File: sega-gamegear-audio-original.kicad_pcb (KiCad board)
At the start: 2 copper layers, 57 x 31 mm, 20 parts, among them CN1 CONN 2P, CN2 292161-6, IC1 Val**, J1 CONN MINI JACK

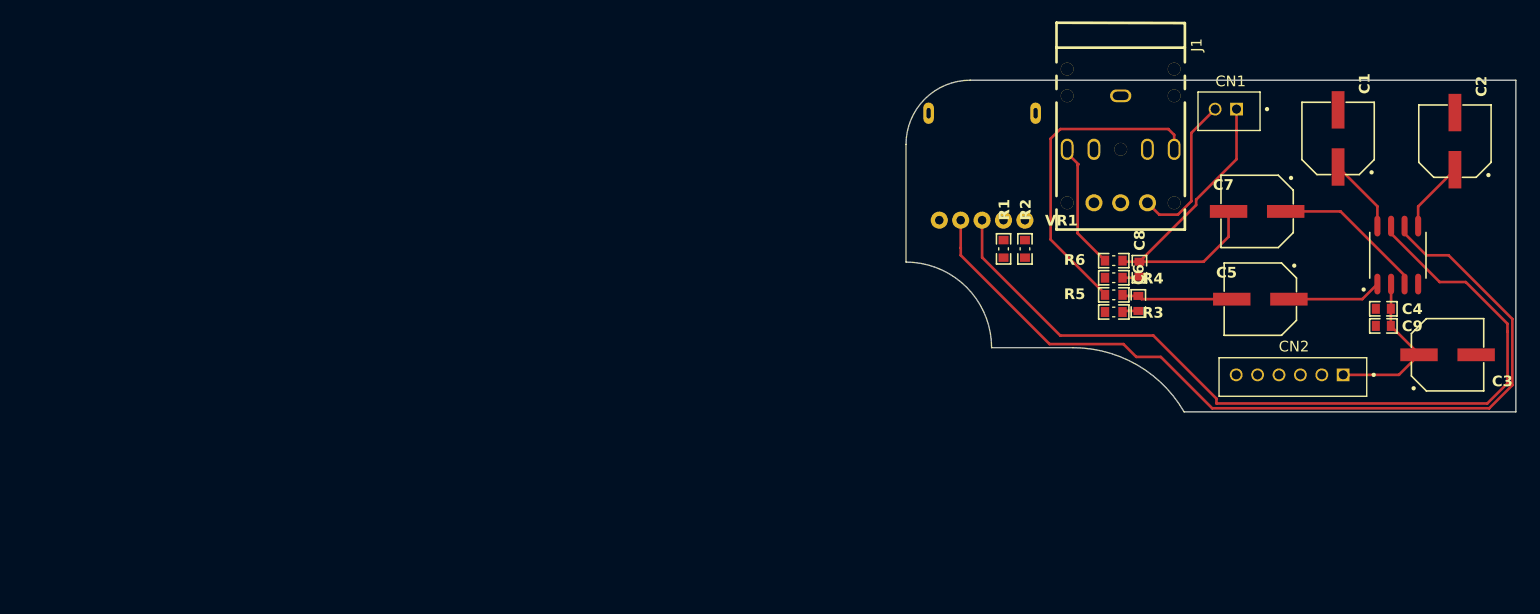
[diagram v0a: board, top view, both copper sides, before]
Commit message: add plated through holes
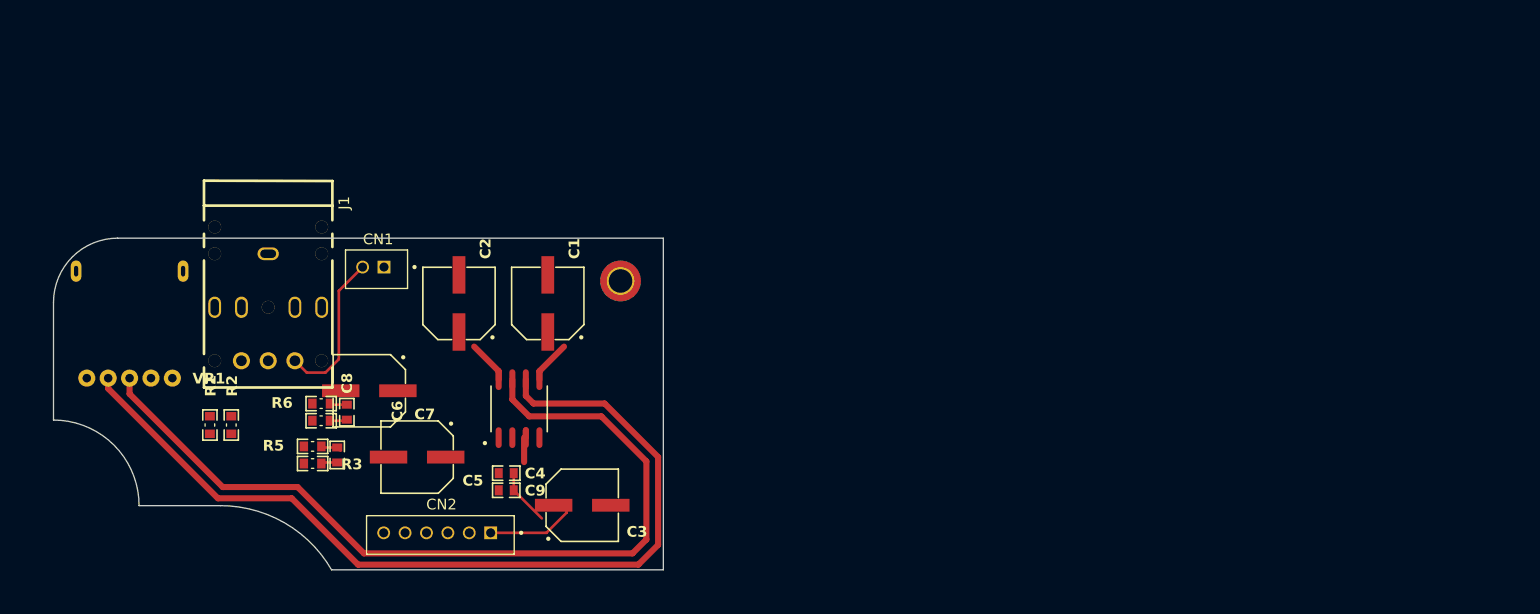
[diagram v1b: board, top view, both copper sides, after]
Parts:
- added REF**: MountingHole_2.2mm_M2_DIN965_Pad_TopBottom, Sega GameGear Audio Board Original:MountingHoleM2, F.Cu at (96.0, 104.0)
- moved C2 94.3 mm to (80.9, 106.1)
- moved C7 84.7 mm to (72.5, 114.3)
- moved C4 83.4 mm to (85.3, 122.0)
- moved C9 83.4 mm to (85.3, 123.6)
- moved IC1 83.4 mm to (86.5, 116.0)
- moved C3 82.1 mm to (92.4, 125.0)
- moved CN2 81.0 mm to (83.9, 127.5)
- moved VR1 81.0 mm to (50.1, 103.1)
- moved CN1 81.0 mm to (73.9, 102.7)
- moved J1 81.0 mm to (63.1, 106.5)
- moved C5 80.2 mm to (77.0, 120.5)
- moved C6 76.2 mm to (69.5, 120.3)
- moved R3 76.2 mm to (67.2, 121.1)
- moved R5 76.2 mm to (67.2, 119.5)
- moved R1 76.0 mm to (57.6, 117.5)
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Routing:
- net Net-(J1-Pad3): track 30.2 -> 0.00 mm
- net Net-(CN1-SP+): track 31.3 -> 1.62 mm
- net Net-(J1-Pad2): track 11.9 -> 0.00 mm
- net Net-(IC1-02): track 14.4 -> 3.00 mm
- net Net-(IC1-O1): track 8.86 -> 0.00 mm
- net Net-(C5-Pad2): track 10.4 -> 1.95 mm
- net Net-(IC1--I1): track 7.04 -> 4.04 mm
- net Net-(IC1--I2): track 6.69 -> 4.04 mm
- net Net-(IC1-+I2): track 81.9 -> 84.4 mm
- net Net-(CN2-5V): track 15.6 -> 13.3 mm
- net Net-(IC1-+I1): track 79.9 -> 80.6 mm

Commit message: Initial routing
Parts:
- added ?: , , F.Cu at (54.0, 122.0)
- added REF**: MountingHole_2.2mm_M2_DIN965_Pad_TopBottom, Sega GameGear Audio Board Original:MountingHoleM2, F.Cu at (54.0, 122.0)
- moved C2 12.3 mm to (92.7, 109.7)
- moved C5 8.41 mm to (77.9, 112.1)
- moved C7 8.16 mm to (77.9, 120.4)
- moved C9 6.91 mm to (90.5, 119.0), turned to 180 degrees
- moved C4 6.91 mm to (90.5, 117.4), turned to 180 degrees
- moved R1 5.06 mm to (53.0, 115.4)
- moved R2 5.06 mm to (55.0, 115.4)
- moved C1 4.93 mm to (84.3, 105.6)
- moved R4 4.35 mm to (68.3, 121.4)
- moved C8 4.15 mm to (70.8, 120.4)
- moved R6 4.05 mm to (68.3, 119.5)
- moved R3 3.51 mm to (67.8, 117.6)
- moved C6 3.51 mm to (70.1, 116.8)
- moved R5 3.51 mm to (67.8, 116.0)
- moved CN1 3.01 mm to (76.9, 102.8)
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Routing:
- net Net-(CN1-SP+): track 1.62 -> 27.3 mm
- net Net-(CN2-SPON): track 0.00 -> 20.0 mm
- net Net-(J1-Pad2): track 0.00 -> 19.1 mm
- net Net-(J1-Pad3): track 0.00 -> 14.2 mm
- net Net-(IC1-O1): track 0.00 -> 8.30 mm
- net Net-(CN2-5V): track 13.3 -> 21.6 mm
- net Net-(C5-Pad2): track 1.95 -> 10.1 mm
- net Net-(IC1-02): track 3.00 -> 7.15 mm
- net Net-(IC1-+I2): track 84.4 -> 87.1 mm
- net Net-(IC1-+I1): track 80.6 -> 82.4 mm
- net Net-(CN1-SP-): track 14.6 -> 13.2 mm
- net Net-(IC1--I1): track 4.04 -> 5.44 mm
- net Net-(IC1--I2): track 4.04 -> 5.42 mm

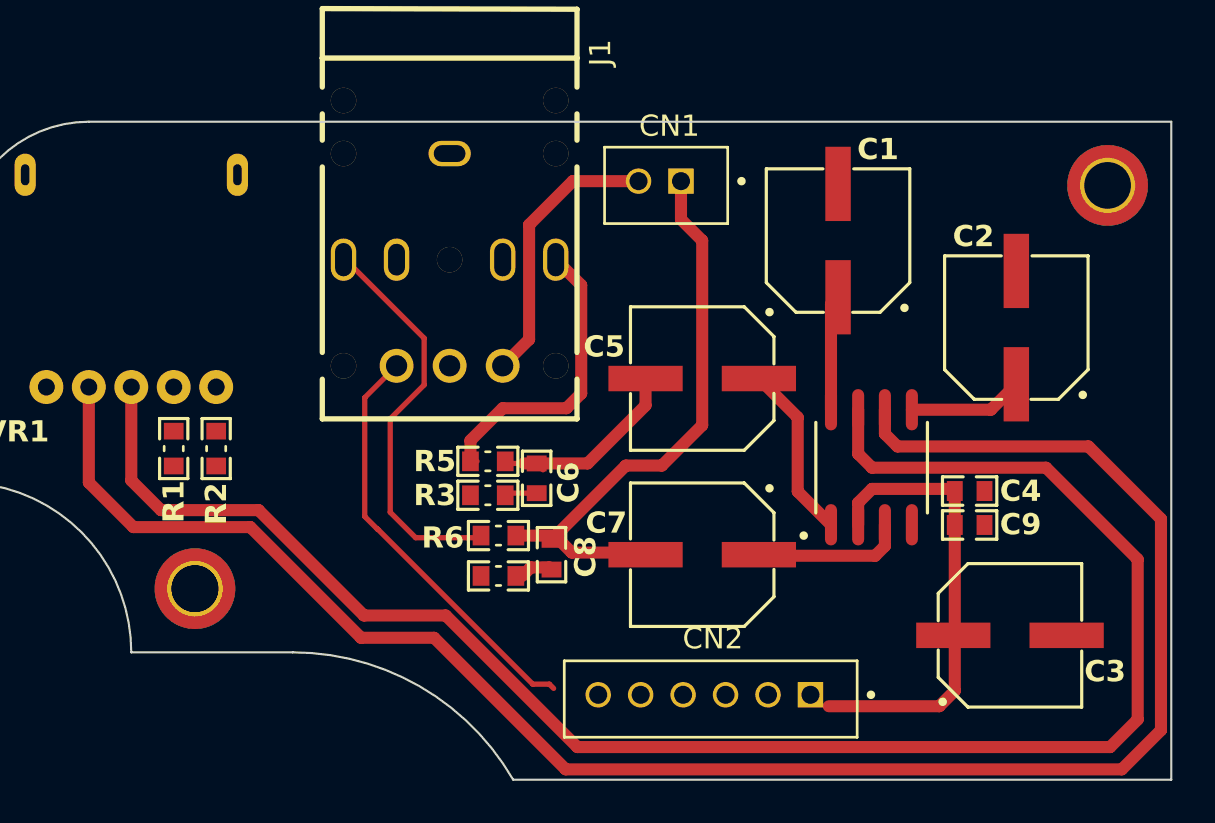
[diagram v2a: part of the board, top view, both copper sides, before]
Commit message: add vias
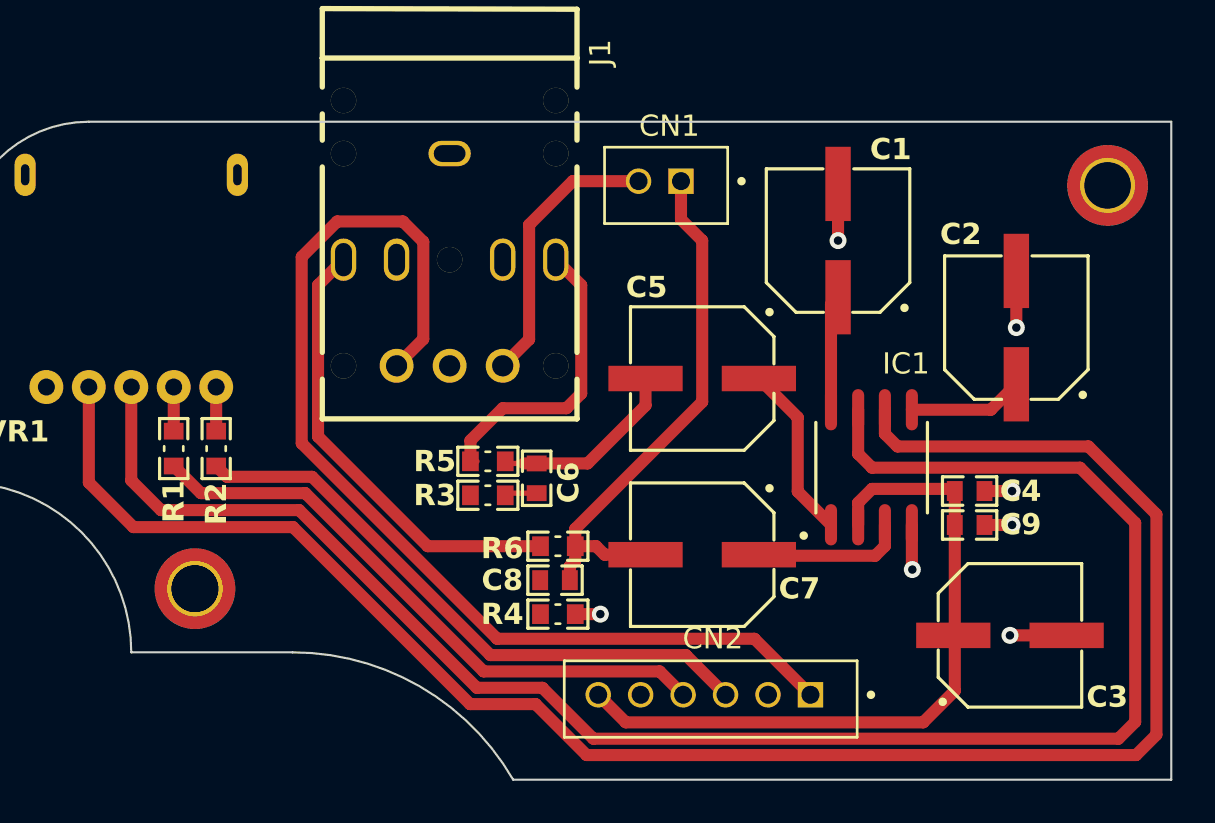
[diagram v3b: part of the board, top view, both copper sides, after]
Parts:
- moved R4 3.33 mm to (71.1, 123.2), turned to 180 degrees
- moved R6 2.84 mm to (71.1, 120.0)
- moved C8 1.21 mm to (71.0, 121.6), turned to 0 degrees
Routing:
- net Net-(CN2-SPON): track 20.0 -> 50.8 mm
- net Net-(CN2-RIN): track 0.00 -> 28.5 mm
- net Net-(CN2-LIN): track 0.00 -> 28.5 mm
- net GND: track 0.00 -> 13.9 mm, vias 0 -> 7
- net Net-(CN2-5V): track 21.6 -> 33.3 mm
- net Net-(J1-Pad2): track 19.1 -> 21.6 mm
- net Net-(R2-Pad2): track 0.00 -> 2.08 mm
- net Net-(R1-Pad2): track 0.00 -> 2.08 mm
- net Net-(CN1-SP+): track 27.3 -> 25.7 mm
- net Net-(C8-Pad1): track 1.59 -> 0.00 mm
- net Net-(IC1-+I2): track 87.1 -> 86.4 mm
- net Net-(IC1-+I1): track 82.4 -> 82.9 mm

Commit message: trace sizing
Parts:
- moved C6 3.44 mm to (66.7, 116.9), turned to 0 degrees
- moved R3 1.35 mm to (66.8, 118.5), turned to 180 degrees
- moved R5 1.22 mm to (66.8, 115.3)
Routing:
- net Net-(C5-Pad2): track 9.65 -> 11.5 mm
- net Net-(C8-Pad1): track 0.00 -> 1.61 mm
- net GND: track 13.9 -> 15.1 mm, vias 7 -> 8
- net Net-(IC1-+I2): track 86.4 -> 85.7 mm
- net Net-(IC1-+I1): track 82.9 -> 82.3 mm

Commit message: trace sizing
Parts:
- CN1: value CONN 2P -> 292161-6; footprint Sega GameGear Audio Board Original:292161-2 -> Sega GameGear Audio Board Original:292161-6
- CN2: value 292161-6 -> CONN 2P; footprint Sega GameGear Audio Board Original:292161-6 -> Sega GameGear Audio Board Original:292161-2
- IC1: value Val** -> TDA2822D
- moved CN1 25.0 mm to (83.0, 127.0)
- moved CN2 24.9 mm to (76.8, 102.9)
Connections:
- C3 pad 1: Net-(CN2-5V) -> Net-(CN1-5V)
- C4 pad 2: Net-(CN2-5V) -> Net-(CN1-5V)
- C7 pad 2: Net-(CN1-SP+) -> Net-(CN2-SP+)
- C8 pad 2: Net-(CN1-SP+) -> Net-(CN2-SP+)
- C9 pad 2: Net-(CN2-5V) -> Net-(CN1-5V)
- CN1 pad 1: Net-(CN1-SP+) -> Net-(CN1-5V)
- CN1 pad 2: Net-(CN1-SP-) -> GND
- CN2 pad 1: Net-(CN2-5V) -> Net-(CN2-SP+)
- CN2 pad 2: GND -> Net-(CN2-SP-)
- IC1 pad 2: Net-(CN2-5V) -> Net-(CN1-5V)
- J1 pad 4: Net-(CN1-SP-) -> Net-(CN2-SP-)
- J1 pad 6: Net-(CN2-SPON) -> Net-(CN1-SPON)
- R1 pad 1: Net-(CN2-RIN) -> Net-(CN1-RIN)
- R2 pad 1: Net-(CN2-LIN) -> Net-(CN1-LIN)
- R6 pad 1: Net-(CN1-SP+) -> Net-(CN2-SP+)
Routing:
- net Net-(CN2-SPON): track 50.8 -> 0.00 mm
- net Net-(CN1-SPON): track 0.00 -> 50.8 mm
- net Net-(CN2-5V): track 33.3 -> 0.00 mm
- net Net-(CN1-5V): track 0.00 -> 33.3 mm
- net Net-(CN2-RIN): track 28.5 -> 0.00 mm
- net Net-(CN1-RIN): track 0.00 -> 28.5 mm
- net Net-(CN2-LIN): track 28.5 -> 0.00 mm
- net Net-(CN1-LIN): track 0.00 -> 28.5 mm
- net Net-(CN2-SP+): track 0.00 -> 25.7 mm
- net Net-(CN1-SP+): track 25.7 -> 0.00 mm
- net Net-(CN2-SP-): track 0.00 -> 13.2 mm
- net Net-(CN1-SP-): track 13.2 -> 0.00 mm
- added copper zone on B.Cu, net GND

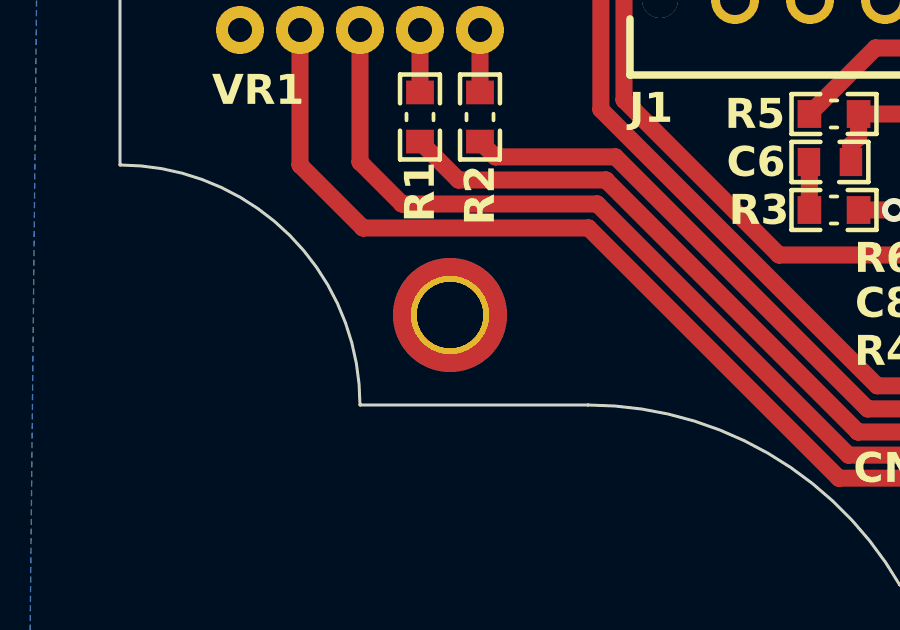
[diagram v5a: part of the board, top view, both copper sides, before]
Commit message: fixes #4 silkscreen issues
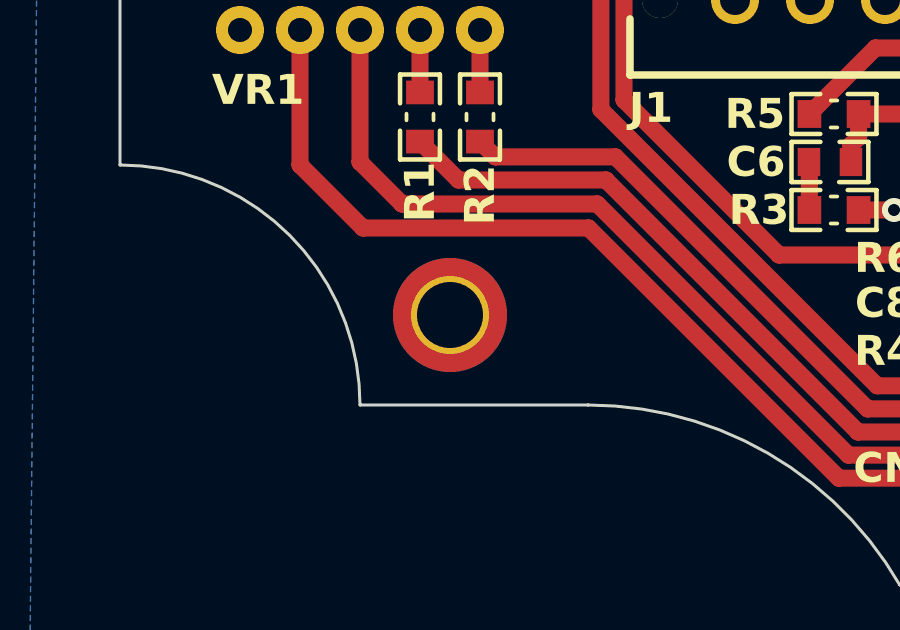
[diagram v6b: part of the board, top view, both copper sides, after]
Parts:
- removed ?: , 
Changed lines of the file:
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@@
     )
-  )
-  (footprint "" locked (layer "F.Cu")
-    (at 54 122)
-    (fp_text reference "" (at 0 0) (layer "F.SilkS")
-        (effects (font (size 1.27 1.27) (thickness 0.15)))
-    )
-    (fp_text value "" (at 0 0) (layer "F.SilkS")
-        (effects (font (size 1.27 1.27) (thickness 0.15)))
-    )
-    (pad "1" thru_hole circle locked (at 0 0) (size 2.6 2.6) (drill 2.2) (layers "*.Cu" "*.Mask"))
   )
   (footprint "Sega GameGear Audio Board Original:C63D" (layer "F.Cu")

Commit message: fix drc
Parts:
- IC1: value TDA2822D -> Val**
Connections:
- REF** pad 1: (no net) -> GND (x2)

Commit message: add production files
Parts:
- IC1: value Val** -> TDA2822D
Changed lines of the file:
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@@
     (at 92.7 109.7 90)
     (property "Height" "7.8")
+    (property "LCSC Part" "C494824")
     (property "Manufacturer_Name" "Panasonic")
     (property "Manufacturer_Part_Number" "EEEFN1E101UP")
@@
     (tags "Capacitor")
     (property "Height" "0.9")
+    (property "LCSC Part" "C3011705")
     (property "Manufacturer_Name" "Murata Electronics")
     (property "Manufacturer_Part_Number" "GRM188R72A104KA35J")
@@
     (tags "Capacitor")
     (property "Height" "0.9")
+    (property "LCSC Part" "C3011705")
     (property "Manufacturer_Name" "Murata Electronics")
     (property "Manufacturer_Part_Number" "GRM188R72A104KA35J")
@@
     (at 77.9 112.1 180)
     (property "Height" "7.8")
+    (property "LCSC Part" "C336261")
     (property "Manufacturer_Name" "Panasonic")
     (property "Manufacturer_Part_Number" "EEEFK1C470P")
@@
     (property "Sheetfile" "sega-gamegear-audio-original.kicad_sch")
     (property "Sheetname" "")
-    (attr through_hole)
+    (attr through_hole exclude_from_pos_files)
     (fp_text reference "J1" (at 8.6 5.3) (layer "F.SilkS")
         (effects (font (size 1 1) (thickness 0.2) bold))
     )
-    (fp_text value "CONN MINI JACK" (at 0 9 -90) (layer "F.Fab") hide
+    (fp_text value "CONN MINI JACK" (at 0 9 90) (layer "F.Fab") hide
         (effects (font (size 1 1) (thickness 0.15)))
     )
@@
     (tags "Capacitor")
     (property "Height" "0.9")
+    (property "LCSC Part" "C3011705")
     (property "Manufacturer_Name" "Murata Electronics")
     (property "Manufacturer_Part_Number" "GRM188R72A104KA35J")
@@
         (effects (font (size 1 1) (thickness 0.2) bold))
     )
-    (fp_text value "Val**" (at 0 4.025 90) (layer "F.SilkS") hide
+    (fp_text value "TDA2822D" (at 0 4.025 90) (layer "F.SilkS") hide
         (effects (font (size 1.27 1.27) (thickness 0.15)))
     )
@@
     (at 84.3 105.6 90)
     (property "Height" "7.8")
+    (property "LCSC Part" "C494824")
     (property "Manufacturer_Name" "Panasonic")
     (property "Manufacturer_Part_Number" "EEEFN1E101UP")
@@
     (property "ki_description" "Panasonic EVUTV2B19A14")
     (property "ki_keywords" "resistor variable")
-    (attr smd)
+    (attr smd exclude_from_pos_files)
     (fp_text reference "VR1" (at -3.4 12 unlocked) (layer "F.SilkS")
         (effects (font (size 1 1) (thickness 0.2) bold))
@@
     (at 92.4 124.2)
     (property "Height" "7.8")
+    (property "LCSC Part" "C178586")
     (property "Manufacturer_Name" "Panasonic")
     (property "Manufacturer_Part_Number" "EEEFT0J331AP")
@@
     (property "Sheetfile" "sega-gamegear-audio-original.kicad_sch")
     (property "Sheetname" "")
-    (attr through_hole)
+    (attr through_hole exclude_from_pos_files)
     (fp_text reference "CN1" (at -14 0.1) (layer "F.SilkS")
         (effects (font (size 1 1) (thickness 0.2) bold))
@@
     (property "Sheetfile" "sega-gamegear-audio-original.kicad_sch")
     (property "Sheetname" "")
-    (attr through_hole)
+    (attr through_hole exclude_from_pos_files)
     (fp_text reference "CN2" (at 0.9 2.9) (layer "F.SilkS")
         (effects (font (size 1 1) (thickness 0.2) bold))
@@
     (at 77.9 120.4 180)
     (property "Height" "7.8")
+    (property "LCSC Part" "C336261")
     (property "Manufacturer_Name" "Panasonic")
     (property "Manufacturer_Part_Number" "EEEFK1C470P")
